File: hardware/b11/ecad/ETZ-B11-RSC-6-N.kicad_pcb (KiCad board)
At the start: 2 copper layers, 131.5 x 85.8 mm, 44 parts, among them SW1 MX-Hotswap-1U, SW10 MX-Hotswap-1U, SW11 MX-Hotswap-1U, SW12 MX-Hotswap-1U, SW13 MX-Hotswap-1U, SW14 MX-Hotswap-1U, SW15 MX-Hotswap-1U, SW16 MX-Hotswap-1U, SW17 MX-Hotswap-1U, SW18 MX-Hotswap-1U, SW19 MX-Hotswap-1U, SW2 MX-Hotswap-1U, SW20 MX-Hotswap-1U, SW21 MX-Hotswap-1U, SW22 MX-Hotswap-1U, SW3 MX-Hotswap-1U, SW4 MX-Hotswap-1U, SW5 MX-Hotswap-1U, SW6 MX-Hotswap-1U, SW7 MX-Hotswap-1U, SW8 MX-Hotswap-1U, SW9 MX-Hotswap-1U

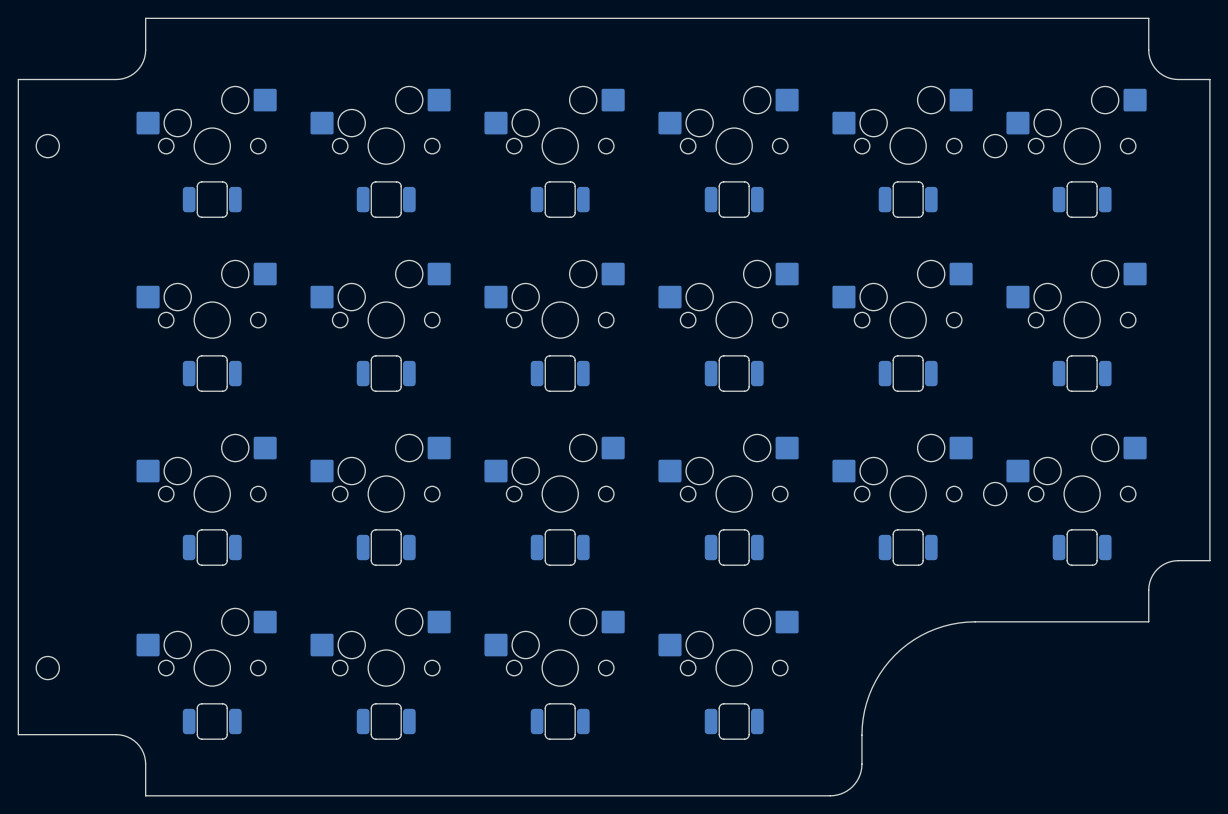
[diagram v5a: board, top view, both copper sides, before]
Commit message: fix(hardware/b11): adjust LED offset to 5.0mm and regenerate all carrier PCBs
Reduces south-facing LED offset from 5.9mm to 5.0mm (closer to the
standard 5.08mm switch-to-LED spacing). All 8 carrier PCBs regenerated.

Co-Authored-By: Claude Sonnet 4.6 <noreply@anthropic.com>
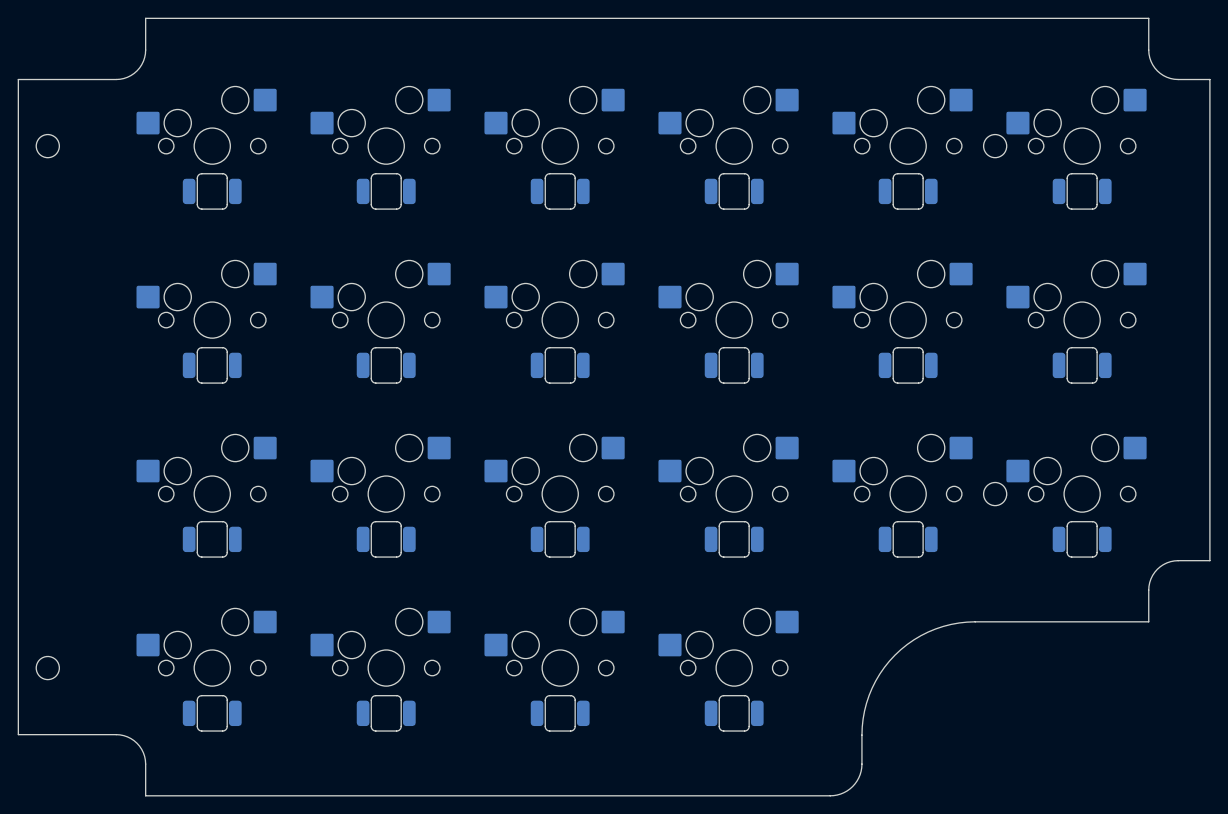
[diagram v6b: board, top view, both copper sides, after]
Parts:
- moved LED13 0.90 mm to (200.2, 116.7)
- moved LED14 0.90 mm to (180.9, 116.7)
- moved LED15 0.90 mm to (161.8, 116.7)
- moved LED16 0.90 mm to (142.6, 116.7)
- moved LED17 0.90 mm to (123.3, 116.7)
- moved LED18 0.90 mm to (104.2, 116.7)
- moved LED1 0.90 mm to (200.2, 78.3)
- moved LED10 0.90 mm to (142.6, 97.5)
- moved LED11 0.90 mm to (123.3, 97.5)
- moved LED12 0.90 mm to (104.2, 97.5)
- moved LED19 0.90 mm to (161.8, 135.9)
- moved LED2 0.90 mm to (180.9, 78.3)
- moved LED20 0.90 mm to (142.6, 135.9)
- moved LED21 0.90 mm to (123.3, 135.9)
- moved LED22 0.90 mm to (104.2, 135.9)
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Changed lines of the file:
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@@
 	(footprint "LED_SMD_6028_BackMount"
 		(layer "B.Cu")
-		(at 161.75 98.4)
+		(at 123.35 116.699999)
 		(descr "SMD 6028 back-paste reverse-mount LED, 5.88x2.80mm body, 3.20mm lens, slot 3.3x6.2mm")
 		(tags "LED SMD 6028 reverse-mount back-paste backlighting Choc")
-		(property "Reference" "LED9"
+		(property "Reference" "LED17"
 			(at 0 -2 0)
 			(layer "B.Fab")
@@
 	(footprint "LED_SMD_6028_BackMount"
 		(layer "B.Cu")
-		(at 200.15 79.2)
+		(at 123.35 135.899999)
 		(descr "SMD 6028 back-paste reverse-mount LED, 5.88x2.80mm body, 3.20mm lens, slot 3.3x6.2mm")
 		(tags "LED SMD 6028 reverse-mount back-paste backlighting Choc")
-		(property "Reference" "LED1"
+		(property "Reference" "LED21"
 			(at 0 -2 0)
 			(layer "B.Fab")
@@
 	(footprint "LED_SMD_6028_BackMount"
 		(layer "B.Cu")
-		(at 142.55 79.2)
+		(at 161.75 97.5)
 		(descr "SMD 6028 back-paste reverse-mount LED, 5.88x2.80mm body, 3.20mm lens, slot 3.3x6.2mm")
 		(tags "LED SMD 6028 reverse-mount back-paste backlighting Choc")
-		(property "Reference" "LED4"
+		(property "Reference" "LED9"
 			(at 0 -2 0)
 			(layer "B.Fab")
@@
 	(footprint "LED_SMD_6028_BackMount"
 		(layer "B.Cu")
-		(at 104.15 117.6)
+		(at 142.55 116.699999)
 		(descr "SMD 6028 back-paste reverse-mount LED, 5.88x2.80mm body, 3.20mm lens, slot 3.3x6.2mm")
 		(tags "LED SMD 6028 reverse-mount back-paste backlighting Choc")
-		(property "Reference" "LED18"
+		(property "Reference" "LED16"
 			(at 0 -2 0)
 			(layer "B.Fab")
@@
 	(footprint "LED_SMD_6028_BackMount"
 		(layer "B.Cu")
-		(at 123.35 79.2)
+		(at 104.15 116.699999)
 		(descr "SMD 6028 back-paste reverse-mount LED, 5.88x2.80mm body, 3.20mm lens, slot 3.3x6.2mm")
 		(tags "LED SMD 6028 reverse-mount back-paste backlighting Choc")
-		(property "Reference" "LED5"
+		(property "Reference" "LED18"
 			(at 0 -2 0)
 			(layer "B.Fab")
@@
 	(footprint "LED_SMD_6028_BackMount"
 		(layer "B.Cu")
-		(at 123.35 98.4)
+		(at 180.95 116.699999)
 		(descr "SMD 6028 back-paste reverse-mount LED, 5.88x2.80mm body, 3.20mm lens, slot 3.3x6.2mm")
 		(tags "LED SMD 6028 reverse-mount back-paste backlighting Choc")
-		(property "Reference" "LED11"
+		(property "Reference" "LED14"
 			(at 0 -2 0)
 			(layer "B.Fab")
@@
 	(footprint "LED_SMD_6028_BackMount"
 		(layer "B.Cu")
-		(at 123.35 117.6)
+		(at 200.15 116.699999)
 		(descr "SMD 6028 back-paste reverse-mount LED, 5.88x2.80mm body, 3.20mm lens, slot 3.3x6.2mm")
 		(tags "LED SMD 6028 reverse-mount back-paste backlighting Choc")
-		(property "Reference" "LED17"
+		(property "Reference" "LED13"
 			(at 0 -2 0)
 			(layer "B.Fab")
@@
 	(footprint "LED_SMD_6028_BackMount"
 		(layer "B.Cu")
-		(at 142.55 98.4)
+		(at 180.95 97.5)
 		(descr "SMD 6028 back-paste reverse-mount LED, 5.88x2.80mm body, 3.20mm lens, slot 3.3x6.2mm")
 		(tags "LED SMD 6028 reverse-mount back-paste backlighting Choc")
-		(property "Reference" "LED10"
+		(property "Reference" "LED8"
 			(at 0 -2 0)
 			(layer "B.Fab")
@@
 	(footprint "LED_SMD_6028_BackMount"
 		(layer "B.Cu")
-		(at 123.35 136.799999)
+		(at 161.75 78.3)
 		(descr "SMD 6028 back-paste reverse-mount LED, 5.88x2.80mm body, 3.20mm lens, slot 3.3x6.2mm")
 		(tags "LED SMD 6028 reverse-mount back-paste backlighting Choc")
-		(property "Reference" "LED21"
+		(property "Reference" "LED3"
 			(at 0 -2 0)
 			(layer "B.Fab")
@@
 	(footprint "LED_SMD_6028_BackMount"
 		(layer "B.Cu")
-		(at 104.15 136.799999)
+		(at 142.55 97.5)
 		(descr "SMD 6028 back-paste reverse-mount LED, 5.88x2.80mm body, 3.20mm lens, slot 3.3x6.2mm")
 		(tags "LED SMD 6028 reverse-mount back-paste backlighting Choc")
-		(property "Reference" "LED22"
+		(property "Reference" "LED10"
 			(at 0 -2 0)
 			(layer "B.Fab")
@@
 	(footprint "LED_SMD_6028_BackMount"
 		(layer "B.Cu")
-		(at 200.15 98.4)
+		(at 161.75 116.699999)
 		(descr "SMD 6028 back-paste reverse-mount LED, 5.88x2.80mm body, 3.20mm lens, slot 3.3x6.2mm")
 		(tags "LED SMD 6028 reverse-mount back-paste backlighting Choc")
-		(property "Reference" "LED7"
+		(property "Reference" "LED15"
 			(at 0 -2 0)
 			(layer "B.Fab")
@@
 	(footprint "LED_SMD_6028_BackMount"
 		(layer "B.Cu")
-		(at 161.75 117.6)
+		(at 161.75 135.899999)
 		(descr "SMD 6028 back-paste reverse-mount LED, 5.88x2.80mm body, 3.20mm lens, slot 3.3x6.2mm")
 		(tags "LED SMD 6028 reverse-mount back-paste backlighting Choc")
-		(property "Reference" "LED15"
+		(property "Reference" "LED19"
 			(at 0 -2 0)
 			(layer "B.Fab")
@@
 	(footprint "LED_SMD_6028_BackMount"
 		(layer "B.Cu")
-		(at 180.95 79.2)
+		(at 104.15 78.3)
 		(descr "SMD 6028 back-paste reverse-mount LED, 5.88x2.80mm body, 3.20mm lens, slot 3.3x6.2mm")
 		(tags "LED SMD 6028 reverse-mount back-paste backlighting Choc")
-		(property "Reference" "LED2"
+		(property "Reference" "LED6"
 			(at 0 -2 0)
 			(layer "B.Fab")
@@
 	(footprint "LED_SMD_6028_BackMount"
 		(layer "B.Cu")
-		(at 104.15 98.4)
+		(at 200.15 97.5)
 		(descr "SMD 6028 back-paste reverse-mount LED, 5.88x2.80mm body, 3.20mm lens, slot 3.3x6.2mm")
 		(tags "LED SMD 6028 reverse-mount back-paste backlighting Choc")
-		(property "Reference" "LED12"
+		(property "Reference" "LED7"
 			(at 0 -2 0)
 			(layer "B.Fab")
@@
 	(footprint "LED_SMD_6028_BackMount"
 		(layer "B.Cu")
-		(at 161.75 136.799999)
+		(at 104.15 135.899999)
 		(descr "SMD 6028 back-paste reverse-mount LED, 5.88x2.80mm body, 3.20mm lens, slot 3.3x6.2mm")
 		(tags "LED SMD 6028 reverse-mount back-paste backlighting Choc")
-		(property "Reference" "LED19"
+		(property "Reference" "LED22"
 			(at 0 -2 0)
 			(layer "B.Fab")
@@
 	(footprint "LED_SMD_6028_BackMount"
 		(layer "B.Cu")
-		(at 161.75 79.2)
+		(at 142.55 135.899999)
 		(descr "SMD 6028 back-paste reverse-mount LED, 5.88x2.80mm body, 3.20mm lens, slot 3.3x6.2mm")
 		(tags "LED SMD 6028 reverse-mount back-paste backlighting Choc")
-		(property "Reference" "LED3"
+		(property "Reference" "LED20"
 			(at 0 -2 0)
 			(layer "B.Fab")
@@
 	(footprint "LED_SMD_6028_BackMount"
 		(layer "B.Cu")
-		(at 180.95 98.4)
+		(at 104.15 97.5)
 		(descr "SMD 6028 back-paste reverse-mount LED, 5.88x2.80mm body, 3.20mm lens, slot 3.3x6.2mm")
 		(tags "LED SMD 6028 reverse-mount back-paste backlighting Choc")
-		(property "Reference" "LED8"
+		(property "Reference" "LED12"
 			(at 0 -2 0)
 			(layer "B.Fab")
@@
 	(footprint "LED_SMD_6028_BackMount"
 		(layer "B.Cu")
-		(at 142.55 136.799999)
+		(at 123.35 78.3)
 		(descr "SMD 6028 back-paste reverse-mount LED, 5.88x2.80mm body, 3.20mm lens, slot 3.3x6.2mm")
 		(tags "LED SMD 6028 reverse-mount back-paste backlighting Choc")
-		(property "Reference" "LED20"
+		(property "Reference" "LED5"
 			(at 0 -2 0)
 			(layer "B.Fab")
@@
 	(footprint "LED_SMD_6028_BackMount"
 		(layer "B.Cu")
-		(at 104.15 79.2)
+		(at 180.95 78.3)
 		(descr "SMD 6028 back-paste reverse-mount LED, 5.88x2.80mm body, 3.20mm lens, slot 3.3x6.2mm")
 		(tags "LED SMD 6028 reverse-mount back-paste backlighting Choc")
-		(property "Reference" "LED6"
+		(property "Reference" "LED2"
 			(at 0 -2 0)
 			(layer "B.Fab")
@@
 	(footprint "LED_SMD_6028_BackMount"
 		(layer "B.Cu")
-		(at 142.55 117.6)
+		(at 142.55 78.3)
 		(descr "SMD 6028 back-paste reverse-mount LED, 5.88x2.80mm body, 3.20mm lens, slot 3.3x6.2mm")
 		(tags "LED SMD 6028 reverse-mount back-paste backlighting Choc")
-		(property "Reference" "LED16"
+		(property "Reference" "LED4"
 			(at 0 -2 0)
 			(layer "B.Fab")
@@
 	(footprint "LED_SMD_6028_BackMount"
 		(layer "B.Cu")
-		(at 200.15 117.6)
+		(at 123.35 97.5)
 		(descr "SMD 6028 back-paste reverse-mount LED, 5.88x2.80mm body, 3.20mm lens, slot 3.3x6.2mm")
 		(tags "LED SMD 6028 reverse-mount back-paste backlighting Choc")
-		(property "Reference" "LED13"
+		(property "Reference" "LED11"
 			(at 0 -2 0)
 			(layer "B.Fab")
@@
 	(footprint "LED_SMD_6028_BackMount"
 		(layer "B.Cu")
-		(at 180.95 117.6)
+		(at 200.15 78.3)
 		(descr "SMD 6028 back-paste reverse-mount LED, 5.88x2.80mm body, 3.20mm lens, slot 3.3x6.2mm")
 		(tags "LED SMD 6028 reverse-mount back-paste backlighting Choc")
-		(property "Reference" "LED14"
+		(property "Reference" "LED1"
 			(at 0 -2 0)
 			(layer "B.Fab")
